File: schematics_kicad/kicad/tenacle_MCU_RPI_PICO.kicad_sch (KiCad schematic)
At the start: 3 parts, among them T201 tentacle_octobus, T202 tentacle_relay

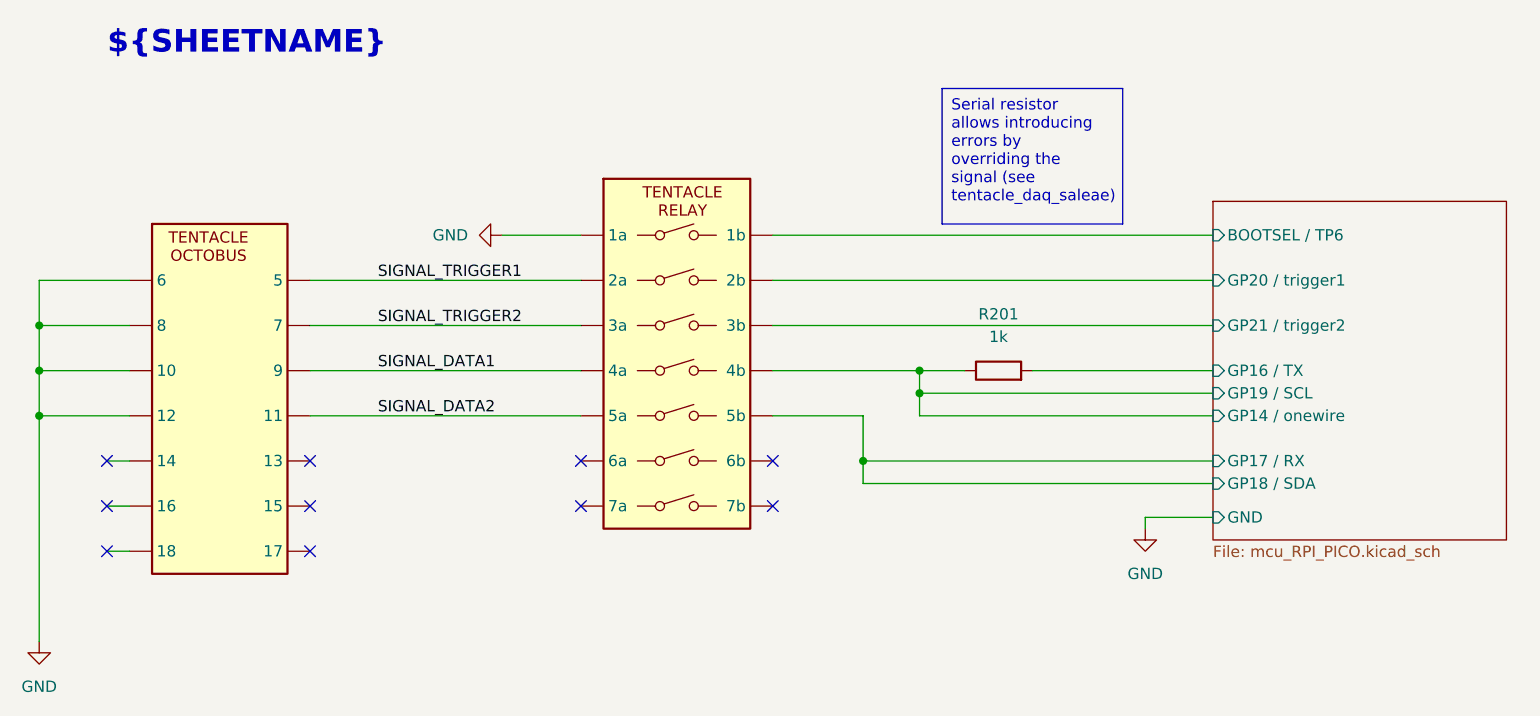
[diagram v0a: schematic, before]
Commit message: FUT_UART_LOOPBACK: LOLIN_D1_MINI, LOLIN_C3_MINI
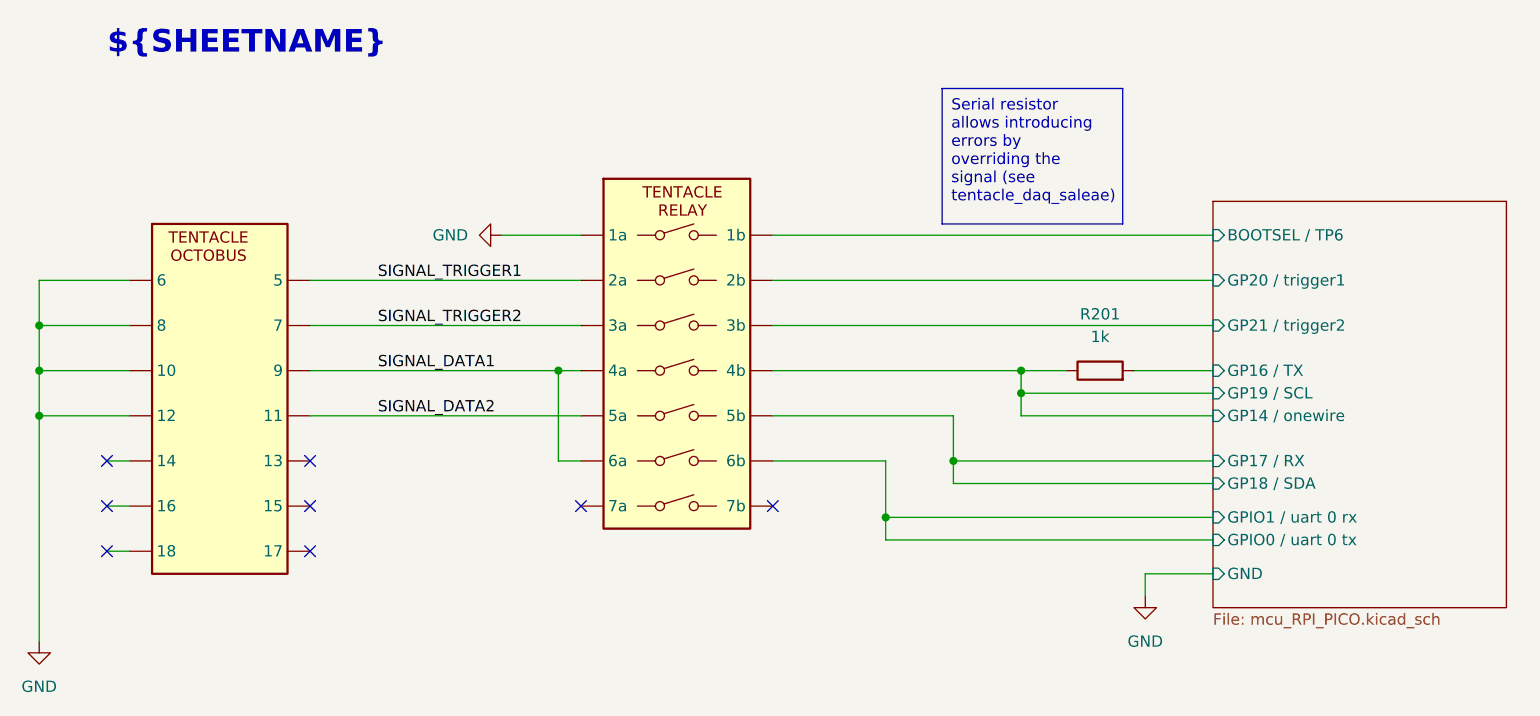
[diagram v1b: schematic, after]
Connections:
- new net MCU_RPI_PICO/GPIO0 / uart 0 tx: T202. (7b)
- no-connect marks 10 -> 8
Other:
- sheet MCU_RPI_PICO ports: added GPIO0 / uart 0 tx, GPIO1 / uart 0 rx; removed none
- moved on the sheet: R201
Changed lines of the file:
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@@
+	)
+	(junction
+		(at 148.59 85.09)
+		(diameter 0)
+		(color 0 0 0 0)
 	)
 	(junction
@@
 	)
 	(junction
-		(at 152.4 71.12)
+		(at 163.83 71.12)
 		(diameter 0)
 		(color 0 0 0 0)
 	)
 	(junction
-		(at 146.05 78.74)
+		(at 111.76 68.58)
 		(diameter 0)
 		(color 0 0 0 0)
 	)
 	(junction
-		(at 152.4 68.58)
+		(at 156.21 78.74)
 		(diameter 0)
 		(color 0 0 0 0)
 	)
-	(no_connect
-		(at 135.89 78.74)
+	(junction
+		(at 163.83 68.58)
+		(diameter 0)
+		(color 0 0 0 0)
 	)
 	(no_connect
@@
 	)
 	(no_connect
-		(at 114.3 78.74)
-	)
-	(no_connect
 		(at 60.96 88.9)
 	)
@@
 	(wire
 		(pts
-			(xy 146.05 81.28) (xy 185.42 81.28)
+			(xy 156.21 81.28) (xy 185.42 81.28)
+		)
+		(stroke
+			(width 0)
+			(type default)
+		)
+	)
+	(wire
+		(pts
+			(xy 111.76 68.58) (xy 114.3 68.58)
 		)
 		(stroke
@@
 	(wire
 		(pts
-			(xy 146.05 78.74) (xy 185.42 78.74)
+			(xy 156.21 78.74) (xy 185.42 78.74)
 		)
 		(stroke
@@
 	(wire
 		(pts
-			(xy 135.89 68.58) (xy 152.4 68.58)
-		)
-		(stroke
-			(width 0)
-			(type default)
-		)
-	)
-	(wire
-		(pts
-			(xy 177.8 85.09) (xy 177.8 86.36)
-		)
-		(stroke
-			(width 0)
-			(type default)
-		)
-	)
-	(wire
-		(pts
-			(xy 152.4 68.58) (xy 157.48 68.58)
+			(xy 135.89 68.58) (xy 163.83 68.58)
+		)
+		(stroke
+			(width 0)
+			(type default)
+		)
+	)
+	(wire
+		(pts
+			(xy 177.8 91.44) (xy 177.8 93.98)
+		)
+		(stroke
+			(width 0)
+			(type default)
+		)
+	)
+	(wire
+		(pts
+			(xy 163.83 68.58) (xy 168.91 68.58)
 		)
 		(stroke
@@
 	(wire
 		(pts
-			(xy 83.82 68.58) (xy 114.3 68.58)
-		)
-		(stroke
-			(width 0)
-			(type default)
-		)
-	)
-	(wire
-		(pts
-			(xy 146.05 73.66) (xy 146.05 78.74)
-		)
-		(stroke
-			(width 0)
-			(type default)
-		)
-	)
-	(wire
-		(pts
-			(xy 146.05 78.74) (xy 146.05 81.28)
+			(xy 83.82 68.58) (xy 111.76 68.58)
+		)
+		(stroke
+			(width 0)
+			(type default)
+		)
+	)
+	(wire
+		(pts
+			(xy 114.3 78.74) (xy 111.76 78.74)
+		)
+		(stroke
+			(width 0)
+			(type default)
+		)
+	)
+	(wire
+		(pts
+			(xy 156.21 73.66) (xy 156.21 78.74)
+		)
+		(stroke
+			(width 0)
+			(type default)
+		)
+	)
+	(wire
+		(pts
+			(xy 156.21 78.74) (xy 156.21 81.28)
 		)
 		(stroke
@@
 	(wire
 		(pts
-			(xy 135.89 73.66) (xy 146.05 73.66)
-		)
-		(stroke
-			(width 0)
-			(type default)
-		)
-	)
-	(wire
-		(pts
-			(xy 185.42 73.66) (xy 152.4 73.66)
+			(xy 135.89 73.66) (xy 156.21 73.66)
+		)
+		(stroke
+			(width 0)
+			(type default)
+		)
+	)
+	(wire
+		(pts
+			(xy 185.42 73.66) (xy 163.83 73.66)
+		)
+		(stroke
+			(width 0)
+			(type default)
+		)
+	)
+	(wire
+		(pts
+			(xy 148.59 78.74) (xy 148.59 85.09)
 		)
 		(stroke
@@
 	(wire
 		(pts
-			(xy 165.1 68.58) (xy 185.42 68.58)
+			(xy 176.53 68.58) (xy 185.42 68.58)
 		)
 		(stroke
@@
 	(wire
 		(pts
-			(xy 152.4 73.66) (xy 152.4 71.12)
-		)
-		(stroke
-			(width 0)
-			(type default)
-		)
-	)
-	(wire
-		(pts
-			(xy 152.4 71.12) (xy 185.42 71.12)
+			(xy 163.83 73.66) (xy 163.83 71.12)
+		)
+		(stroke
+			(width 0)
+			(type default)
+		)
+	)
+	(wire
+		(pts
+			(xy 163.83 71.12) (xy 185.42 71.12)
 		)
 		(stroke
@@
 	(wire
 		(pts
+			(xy 111.76 78.74) (xy 111.76 68.58)
+		)
+		(stroke
+			(width 0)
+			(type default)
+		)
+	)
+	(wire
+		(pts
+			(xy 135.89 78.74) (xy 148.59 78.74)
+		)
+		(stroke
+			(width 0)
+			(type default)
+		)
+	)
+	(wire
+		(pts
+			(xy 148.59 85.09) (xy 148.59 87.63)
+		)
+		(stroke
+			(width 0)
+			(type default)
+		)
+	)
+	(wire
+		(pts
 			(xy 53.34 63.5) (xy 63.5 63.5)
 		)
@@
 	(wire
 		(pts
-			(xy 152.4 71.12) (xy 152.4 68.58)
-		)
-		(stroke
-			(width 0)
-			(type default)
-		)
-	)
-	(wire
-		(pts
-			(xy 185.42 85.09) (xy 177.8 85.09)
+			(xy 163.83 71.12) (xy 163.83 68.58)
+		)
+		(stroke
+			(width 0)
+			(type default)
+		)
+	)
+	(wire
+		(pts
+			(xy 185.42 91.44) (xy 177.8 91.44)
 		)
 		(stroke
@@
 	(wire
 		(pts
+			(xy 148.59 85.09) (xy 185.42 85.09)
+		)
+		(stroke
+			(width 0)
+			(type default)
+		)
+	)
+	(wire
+		(pts
 			(xy 83.82 58.42) (xy 114.3 58.42)
+		)
+		(stroke
+			(width 0)
+			(type default)
+		)
+	)
+	(wire
+		(pts
+			(xy 185.42 87.63) (xy 148.59 87.63)
 		)
 		(stroke
@@
 	(symbol
 		(lib_id "Device:R")
-		(at 161.29 68.58 90)
+		(at 172.72 68.58 90)
 		(unit 1)
 		(exclude_from_sim no)
@@
 		(fields_autoplaced yes)
 		(property "Reference" "R201"
-			(at 161.29 62.23 90)
+			(at 172.72 62.23 90)
 			(effects
 				(font
@@
 		)
 		(property "Value" "1k"
-			(at 161.29 64.77 90)
+			(at 172.72 64.77 90)
 			(effects
 				(font
@@
 		)
 		(property "Footprint" ""
-			(at 161.29 70.358 90)
+			(at 172.72 70.358 90)
 			(effects
 				(font
@@
 		)
 		(property "Datasheet" "~"
-			(at 161.29 68.58 0)
+			(at 172.72 68.58 0)
 			(effects
 				(font
@@
 		)
 		(property "Description" "Resistor"
-			(at 161.29 68.58 0)
+			(at 172.72 68.58 0)
 			(effects
 				(font
@@
 	(symbol
 		(lib_id "power:GND")
-		(at 177.8 86.36 0)
+		(at 177.8 93.98 0)
 		(unit 1)
 		(exclude_from_sim no)
@@
 		(fields_autoplaced yes)
 		(property "Reference" "#PWR0203"
-			(at 177.8 92.71 0)
+			(at 177.8 100.33 0)
 			(effects
 				(font
@@
 		)
 		(property "Value" "GND"
-			(at 177.8 91.44 0)
+			(at 177.8 99.06 0)
 			(effects
 				(font
@@
 		)
 		(property "Footprint" ""
-			(at 177.8 86.36 0)
+			(at 177.8 93.98 0)
 			(effects
 				(font
@@
 		)
 		(property "Datasheet" ""
-			(at 177.8 86.36 0)
+			(at 177.8 93.98 0)
 			(effects
 				(font
@@
 		)
 		(property "Description" "Power symbol creates a global label with name \"GND\" , ground"
-			(at 177.8 86.36 0)
+			(at 177.8 93.98 0)
 			(effects
 				(font
@@
 	(sheet
 		(at 185.42 49.53)
-		(size 33.02 38.1)
+		(size 33.02 45.72)
 		(fields_autoplaced yes)
 		(stroke
@@
 		)
 		(property "Sheetfile" "mcu_RPI_PICO.kicad_sch"
-			(at 185.42 88.2146 0)
+			(at 185.42 95.8346 0)
 			(effects
 				(font
@@
 		)
 		(pin "GND" input
+			(at 185.42 91.44 180)
+			(effects
+				(font
+					(size 1.27 1.27)
+				)
+				(justify left)
+			)
+		)
+		(pin "GPIO1 {slash} uart 0 rx" input
 			(at 185.42 85.09 180)
 			(effects
 				(font
+					(size 1.27 1.27)
+				)
+				(justify left)
+			)
+		)
+		(pin "GPIO0 {slash} uart 0 tx" input
+			(at 185.42 87.63 180)
+			(effects
+				(font
